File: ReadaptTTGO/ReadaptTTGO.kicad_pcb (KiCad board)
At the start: 2 copper layers, 80 x 115 mm, 101 parts, among them J1 USB_B_Micro, J2 Conn_01x02_Shielded, J3 Micro_SD_Card, J4 Conn_01x13_Female, J5 Conn_01x13_Female, SW1 SW_SPDT, SW2 SW_Push, U1 CP2102N-A01-GQFN24, U2 ESP32, U3 EMH3, U4 TP4054, U5 ME6211, U6 ME6211, U7 662k, U8 OLED-128O064D, U9 RFM69HCW

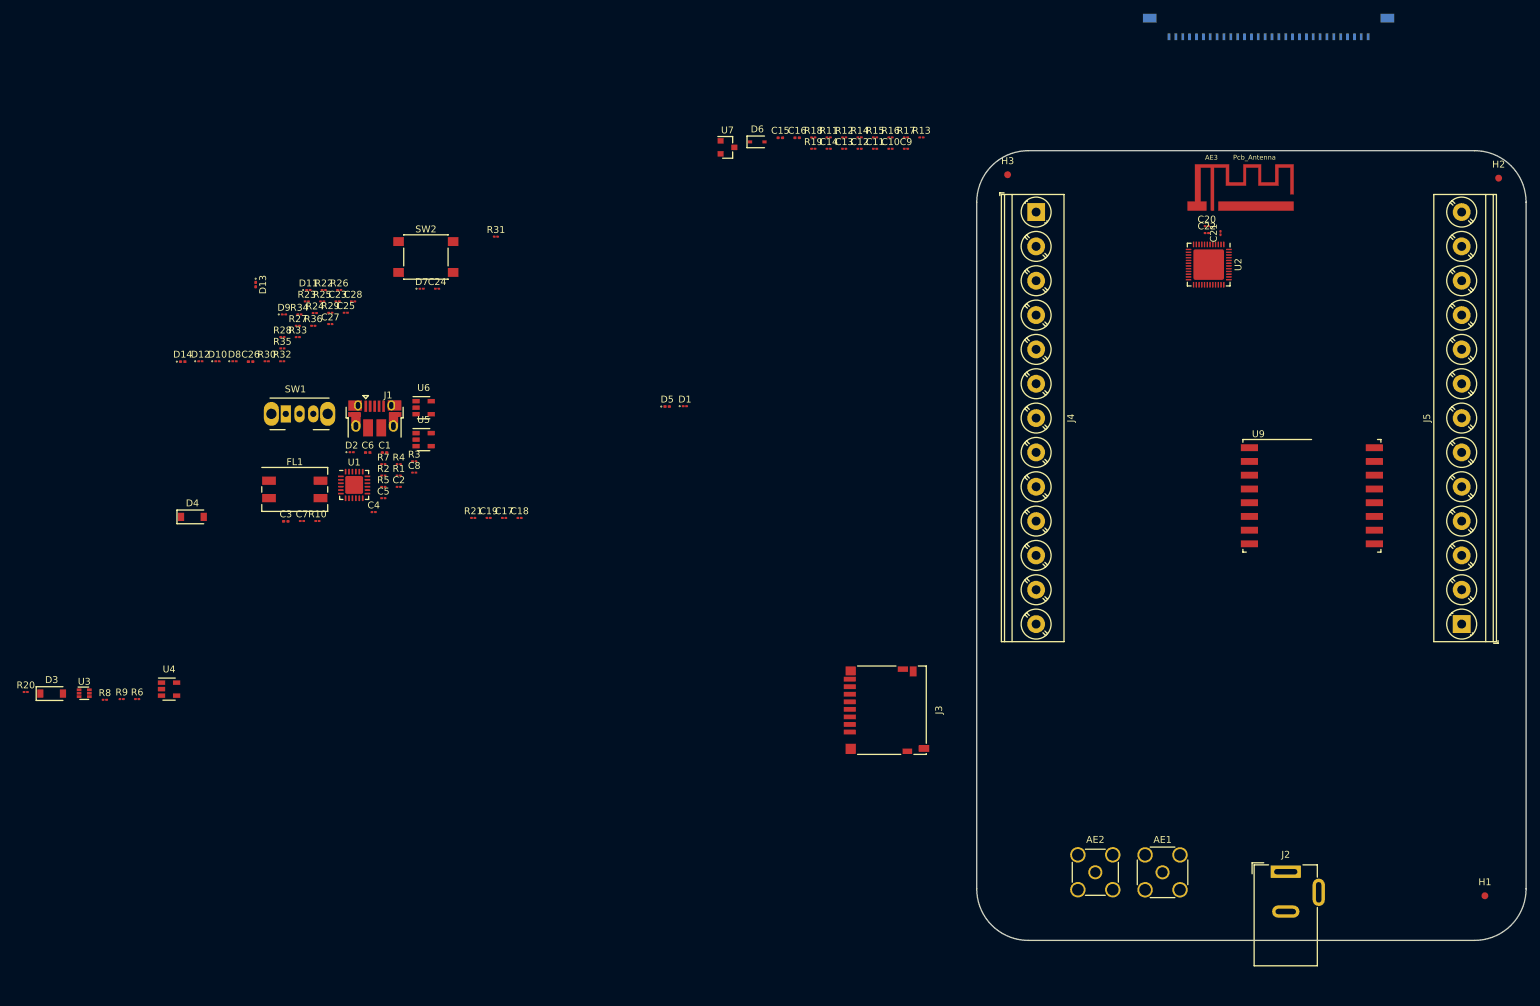
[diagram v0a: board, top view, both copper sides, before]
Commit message: PCB sin traces
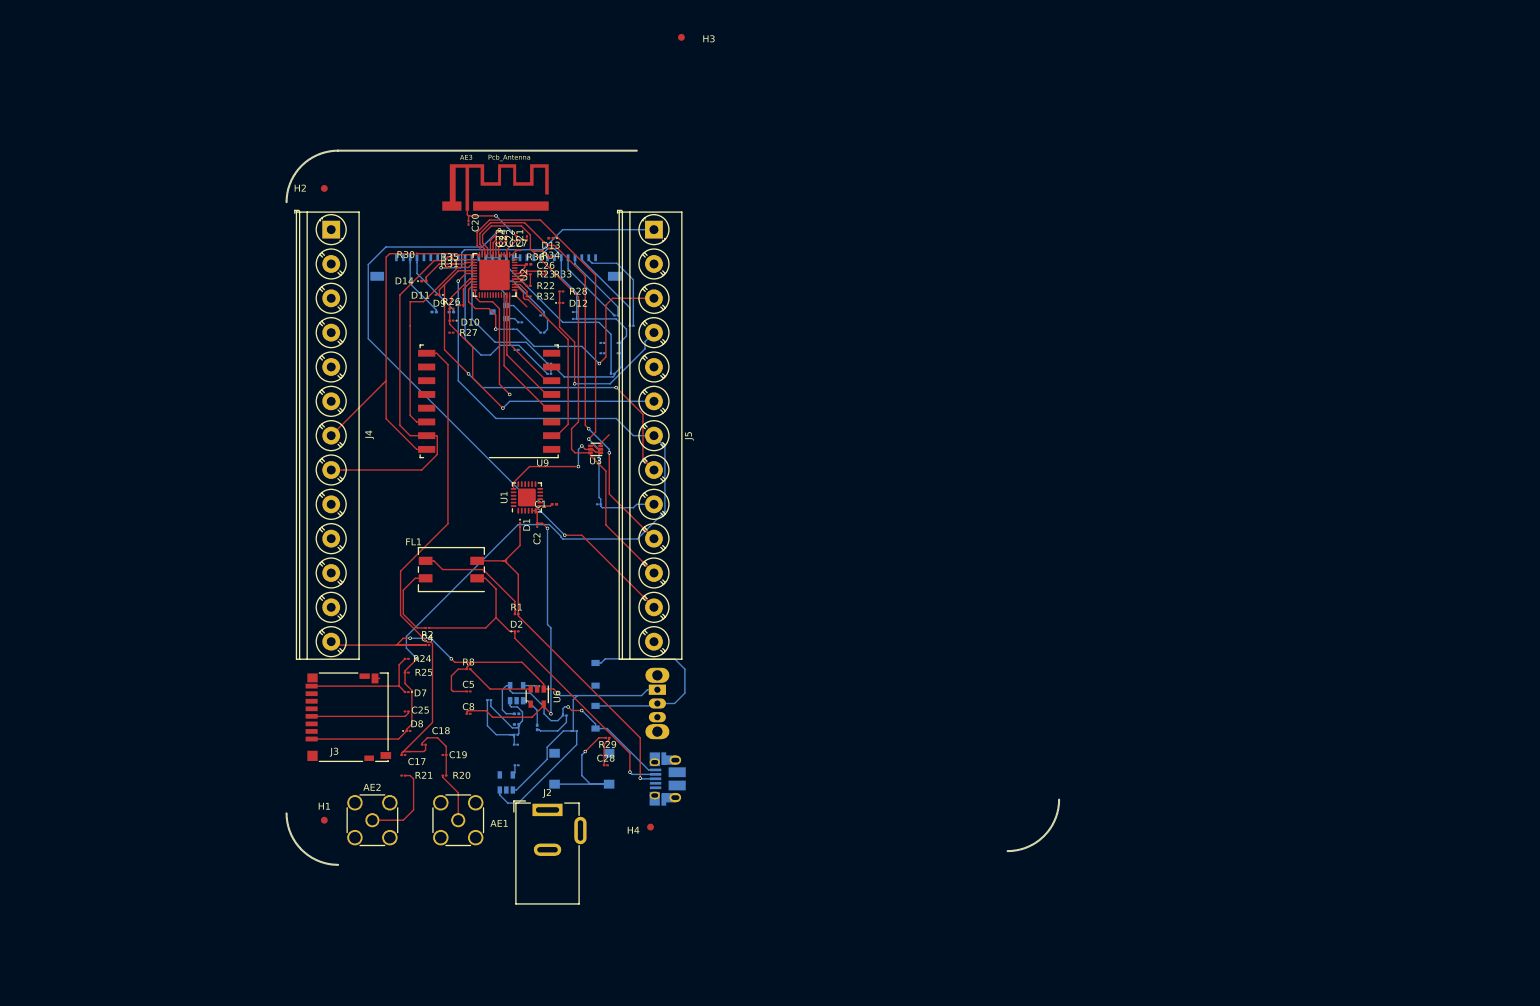
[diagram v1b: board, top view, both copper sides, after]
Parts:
- added H4: MountingHole, Fiducial:Fiducial_1mm_Mask2mm, F.Cu at (110.0, 136.0)
- AE2: footprint Connector_Coaxial:SMA_Amphenol_132134-11_Vertical -> Connector_Coaxial:SMA_Amphenol_132134_Vertical
- C10, C11, C12, C13, C14, C15, C16, C3, C6, C7, C9, D3, D4, D5, D6, J1, R10, R11, R12, R13, R14, R15, R16, R17, R18, R19, R3, R4, R5, R6, R7, R9, SW1, SW2, U4, U5, U7: moved to B.Cu
- moved H2 171.0 mm to (62.5, 43.0)
- moved H1 169.4 mm to (62.5, 135.0)
- moved J5 130.9 mm to (110.5, 49.0), turned to 270 degrees
- moved U9 120.6 mm to (86.5, 74.0), turned to 180 degrees
- moved U8 117.5 mm to (87.5, 54.0), turned to 180 degrees
- moved AE3 108.5 mm to (87.4, 42.9)
- moved J2 107.9 mm to (95.0, 133.5)
- moved C20 107.5 mm to (83.5, 48.0), turned to 270 degrees
- moved AE2 105.5 mm to (69.5, 135.0)
- moved U2 104.0 mm to (87.3, 55.6)
- moved AE1 102.8 mm to (82.0, 135.0)
- moved J4 102.7 mm to (63.5, 49.0)
- moved C21 101.0 mm to (92.0, 50.2)
- moved C22 100.5 mm to (90.5, 50.2), turned to 90 degrees
- moved U3 82.5 mm to (102.0, 81.0), turned to 180 degrees
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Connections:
- C28 pad 1: /micro/RS_EN -> /Power/RST_EN
- R29 pad 1: /micro/RS_EN -> /Power/RST_EN
- R36 pad 2: /micro/RS_EN -> /Power/RST_EN
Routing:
- net /micro/SD2-IO12: track 0.00 -> 138.0 mm, vias 0 -> 2
- net /micro/S_VN: track 0.00 -> 94.1 mm, vias 0 -> 2
- net +5V: track 0.00 -> 88.0 mm, vias 0 -> 3
- net /Power/IO35: track 0.00 -> 78.4 mm, vias 0 -> 1
- net /Power/RST_EN: track 0.00 -> 77.1 mm
- net /moduloRF/ANT: track 0.00 -> 72.7 mm
- net /micro/IO34: track 0.00 -> 65.0 mm, vias 0 -> 2
- net /micro/CLK-SCK-IO14: track 0.00 -> 58.0 mm, vias 0 -> 2
- net /micro/HPDIO1: track 0.00 -> 53.4 mm
- net /Power/D+: track 0.00 -> 53.0 mm, vias 0 -> 1
- net /Power/D-: track 0.00 -> 52.8 mm, vias 0 -> 1
- net VCC: track 0.00 -> 50.8 mm
- net +3.3VP: track 0.00 -> 48.9 mm, vias 0 -> 2
- net /micro/HPDIO2: track 0.00 -> 46.8 mm
- net /micro/SD3-CS-IO13: track 0.00 -> 46.3 mm, vias 0 -> 1
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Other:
- board size 80 x 115 mm -> 112.5 x 104 mm
- board text added: "Esta placa fue desarrollada en lel marco de la materia "Diseño de circuitos impresos" de la Carrera de Especializacion en Sistemas Embebidos de la Uba. En la decicion de posicionamientos de componentes en capas se baso en el diseño original. Grillas: 0.5mm 0.25mm Vias 0.5/0.3mm Margen:0.2mm Pistas: 0.4mm Terminacion: Estaño por inmersion o por OSP"

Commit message: Pre aplicacion de las zonas de relleno
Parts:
- C26, D11, D13, R22, R23, R27, R31, R32, R33, R34: moved to B.Cu
- moved D13 76.6 mm to (88.0, 126.5)
- moved R36 75.4 mm to (103.5, 128.0)
- moved R34 73.1 mm to (88.0, 124.5), turned to 0 degrees
- moved J4 60.0 mm to (62.5, 109.0), turned to 90 degrees
- moved R12 27.8 mm to (80.2, 56.5), turned to 0 degrees
- moved R13 22.1 mm to (77.8, 55.0)
- moved R14 22.1 mm to (77.8, 56.5)
- moved D9 21.5 mm to (104.0, 59.0), turned to 180 degrees
- moved D11 19.0 mm to (98.0, 59.0)
- moved D14 18.8 mm to (95.3, 60.5)
- moved R19 18.7 mm to (75.8, 55.0)
- moved R27 18.2 mm to (98.0, 57.5), turned to 180 degrees
- moved R33 17.2 mm to (77.8, 59.5)
- moved R30 16.6 mm to (90.8, 59.5), turned to 0 degrees
- moved R35 16.3 mm to (95.2, 61.5), turned to 180 degrees
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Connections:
- R22 pad 2: /Power/U0RXD -> /micro/U0RXD
- U1 pad 20: /Power/U0RXD -> /micro/U0RXD
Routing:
- net +3V3: track 27.1 -> 182.4 mm, vias 0 -> 11
- net /micro/SD3-CS-IO13: track 46.3 -> 158.9 mm, vias 1 -> 2
- net /micro/CMD-MOSI-IO15: track 4.62 -> 116.7 mm, vias 0 -> 3
- net /micro/U0RXD: track 0.00 -> 88.5 mm, vias 0 -> 1
- net /micro/SD1-IO4: track 36.7 -> 125.0 mm
- net /micro/SD0-MISO-IO2: track 29.6 -> 112.7 mm, vias 1 -> 3
- net /micro/SD2-IO12: track 138.0 -> 65.4 mm, vias 2 -> 1
- net /micro/IO23: track 15.4 -> 85.7 mm, vias 0 -> 4
- net /micro/S_VP: track 2.62 -> 72.0 mm
- net /micro/CLK-SCK-IO14: track 58.0 -> 123.9 mm
- net /micro/IO21: track 5.16 -> 69.5 mm, vias 0 -> 1
- net /micro/TXD: track 2.07 -> 64.8 mm, vias 0 -> 1
- net /micro/RXD: track 2.04 -> 61.6 mm, vias 0 -> 1
- net /micro/IO19: track 26.8 -> 83.7 mm, vias 0 -> 2
- net /micro/IO22: track 2.93 -> 55.8 mm, vias 0 -> 1
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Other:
- board text added: "Esta placa fue desarrollada en lel marco de la materia "Diseño de circuitos impresos" de la Carrera de Especializacion en Sistemas Embebidos de la Uba. En la decicion de posicionamientos de componentes en capas se baso en el diseño original. Grillas: 0.5mm 0.25mm Vias 0.5/0.3mm 0.8/0.4mm Margen:0.2mm Pistas: 0.4mm Terminacion: Estaño por inmersion o por OSP"
- board text removed: "Esta placa fue desarrollada en lel marco de la materia "Diseño de circuitos impresos" de la Carrera de Especializacion en Sistemas Embebidos de la Uba. En la decicion de posicionamientos de componentes en capas se baso en el diseño original. Grillas: 0.5mm 0.25mm Vias 0.5/0.3mm Margen:0.2mm Pistas: 0.4mm Terminacion: Estaño por inmersion o por OSP"

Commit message: PCB Para revision
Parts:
- added REF**: KiCad-Logo2_5mm_SilkScreen, Symbol:KiCad-Logo2_5mm_SilkScreen, B.Cu at (76.0, 126.5)
- moved H3 21.7 mm to (109.0, 42.0)
- moved H2 1.12 mm to (63.0, 42.0)
- moved J4 1.00 mm to (61.5, 109.0)
- moved C26 0.54 mm to (86.3, 60.8), turned to 180 degrees
- moved C9 0.25 mm to (87.8, 61.0)
- turned C10 to 0 degrees
- turned D13 to 0 degrees
- turned R11 to 0 degrees
- turned R18 to 0 degrees
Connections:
- U2 pad 25: Net-(U2-Pad25) -> GND
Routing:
- net GND: track 8.00 -> 125.7 mm, vias 0 -> 29
- net +5V: track 99.5 -> 208.8 mm, vias 4 -> 7
- net /Power/U0RXD: track 0.00 -> 60.4 mm, vias 0 -> 3
- net +3.3VP: track 92.8 -> 152.1 mm, vias 3 -> 5
- net /micro/SD2-IO12: track 65.4 -> 123.6 mm, vias 1 -> 4
- net +3V3: track 182.4 -> 227.8 mm, vias 11 -> 16
- net +BATT: track 33.9 -> 62.1 mm
- net /Power/IO35: track 100.5 -> 126.0 mm
- net /micro/SD1-IO4: track 125.0 -> 142.1 mm
- net /micro/HPDIO2: track 53.3 -> 68.8 mm, vias 4 -> 5
- net /micro/CMD-MOSI-IO15: track 116.7 -> 131.8 mm
- net /micro/CLK-SCK-IO14: track 123.9 -> 138.9 mm
- net /Power/D+: track 66.5 -> 80.1 mm
- net /micro/U0RXD: track 88.5 -> 102.0 mm
- net /micro/IO23: track 85.7 -> 96.7 mm
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- added copper zone on B.Cu, net GND
- added copper zone on F.Cu, net GND
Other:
- board size 112.5 x 104 mm -> 58.5 x 104 mm
- board text added: "Esta placa fue desarrollada en lel marco de la materia "Diseño de circuitos impresos" de la Carrera de Especializacion en Sistemas Embebidos de la Uba. En la decicion de posicionamientos de componentes en capas se baso en el diseño original. Grillas: 0.5mm 0.25mm Vias: 0.8/0.4mm Margen:0.2mm Pistas: 0.4mm Terminacion: Estaño por inmersion o por OSP"
- board text added: "Ind Arg."
- board text removed: "Esta placa fue desarrollada en lel marco de la materia "Diseño de circuitos impresos" de la Carrera de Especializacion en Sistemas Embebidos de la Uba. En la decicion de posicionamientos de componentes en capas se baso en el diseño original. Grillas: 0.5mm 0.25mm Vias 0.5/0.3mm 0.8/0.4mm Margen:0.2mm Pistas: 0.4mm Terminacion: Estaño por inmersion o por OSP"

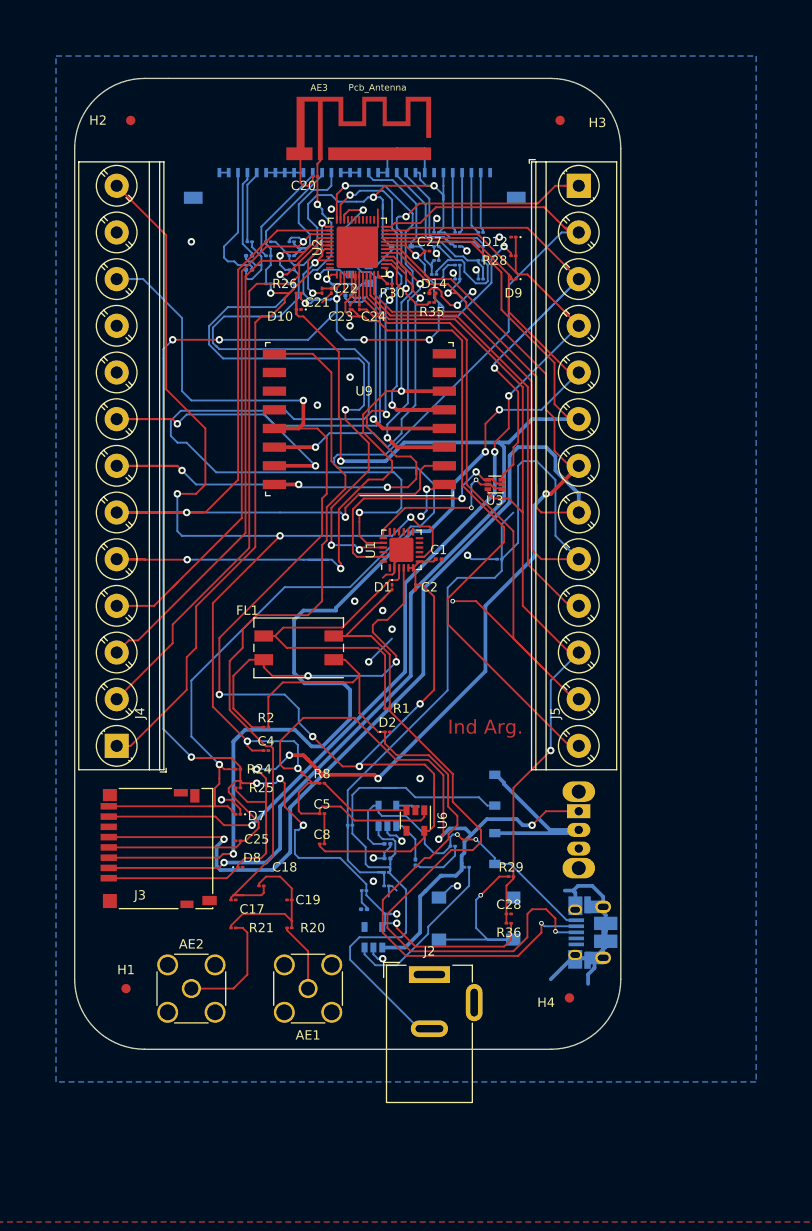
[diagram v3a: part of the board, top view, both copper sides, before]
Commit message: Agregado componentes 3d, serigrafia
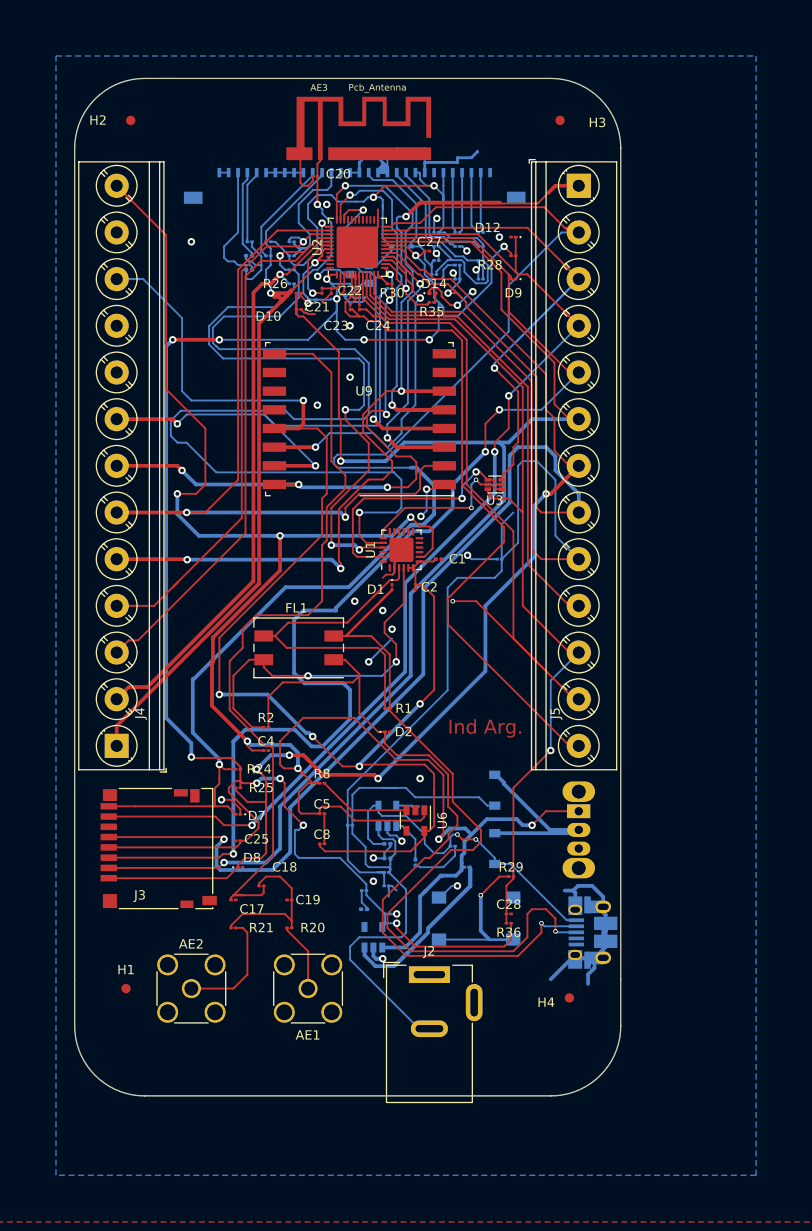
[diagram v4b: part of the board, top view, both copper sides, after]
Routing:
- net /micro/SD1-IO4: track 142.1 -> 167.5 mm
- net /micro/IO23: track 96.7 -> 119.8 mm
- net GND: track 125.7 -> 144.9 mm
- net Net-(R7-Pad2): track 18.4 -> 32.4 mm
- net /micro/IO25: track 37.2 -> 48.6 mm
- net +5V: track 208.8 -> 219.5 mm
- net +3.3VP: track 152.1 -> 160.4 mm
- net /Power/D+: track 80.1 -> 88.4 mm
- net /micro/IO19: track 92.9 -> 98.5 mm
- net /micro/TXD: track 65.2 -> 62.7 mm
- net /Power/DM: track 40.6 -> 39.0 mm
- net /micro/IO21: track 68.5 -> 70.1 mm
- net +3V3: track 227.8 -> 229.2 mm
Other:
- board size 58.5 x 104 mm -> 58.5 x 109 mm
- net class Default: trace_width 0.25 -> 0.2
- net class Exception added: clearance 0.125, trace_width 0.2, via_dia 0.8, via_drill 0.4
- rule pad_to_mask_clearance: 0.051 -> 0.005
- rule solder_mask_min_width: 0.25 -> 0.001
- rule trace_min: 0.2 -> 0.01
- board text added: "Datos del fabricante elegido: Estándares de fabricación Diámetro de agujero 16 (0,40 mm) Diámetro de pad o vía 28 (0,70 mm) Ancho de traza 5 (0,125 mm) Separación entre trazas 5 (0,125 mm) Separación entre traza y pad/vía 5 (0,125 mm) Distancia de cobre a borde 12 (0,30 mm) Altura - trazo de letras 30 - 5"
- board text added: "Esta placa fue desarrollada en lel marco de la materia "Diseño de circuitos impresos" de la Carrera de Especializacion en Sistemas Embebidos de la Uba. En la decicion de posicionamientos de componentes en capas se baso en el diseño original. Grillas: 0.5mm 0.25mm Vias: 0.8/0.4mm Margen:0.2mm Pistas: 0.2mm, 0.4mm Terminacion: Estaño por inmersion o por OSP"
- board text removed: "Esta placa fue desarrollada en lel marco de la materia "Diseño de circuitos impresos" de la Carrera de Especializacion en Sistemas Embebidos de la Uba. En la decicion de posicionamientos de componentes en capas se baso en el diseño original. Grillas: 0.5mm 0.25mm Vias: 0.8/0.4mm Margen:0.2mm Pistas: 0.4mm Terminacion: Estaño por inmersion o por OSP"

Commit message: Entrega revision 1.2
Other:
- board text added: "Ferreyra FeTTGO Rev. 1.2"
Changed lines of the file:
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@@
   (general
     (thickness 1.6)
-    (drawings 16)
+    (drawings 17)
     (tracks 1707)
     (zones 0)
@@
   )
   (setup
-    (last_trace_width 0.4)
+    (last_trace_width 0.2)
     (user_trace_width 0.2)
     (user_trace_width 0.4)
@@
     (tags fiducial)
     (attr smd)
-    (fp_text reference H4 (at -2.5 0.5) (layer F.SilkS)
+    (fp_text reference H4 (at -2.5 0.5) (layer F.SilkS) hide
       (effects (font (size 1 1) (thickness 0.15)))
     )
@@
     (tags fiducial)
     (attr smd)
-    (fp_text reference H3 (at 4 0.25) (layer F.SilkS)
+    (fp_text reference H3 (at 4 0.25) (layer F.SilkS) hide
       (effects (font (size 1 1) (thickness 0.15)))
     )
@@
     (tags fiducial)
     (attr smd)
-    (fp_text reference H2 (at -3.5 0) (layer F.SilkS)
+    (fp_text reference H2 (at -3.5 0) (layer F.SilkS) hide
       (effects (font (size 1 1) (thickness 0.15)))
     )
@@
     (tags fiducial)
     (attr smd)
-    (fp_text reference H1 (at 0 -2) (layer F.SilkS)
+    (fp_text reference H1 (at 0 -2) (layer F.SilkS) hide
       (effects (font (size 1 1) (thickness 0.15)))
     )
@@
     )
   )
+  (gr_text "Ferreyra\nFeTTGO\nRev. 1.2" (at 93.25 125.75) (layer F.SilkS)
+    (effects (font (size 1.5 1.5) (thickness 0.3)))
+  )
   (gr_line (start 57 134) (end 57 139) (layer Edge.Cuts) (width 0.05))
